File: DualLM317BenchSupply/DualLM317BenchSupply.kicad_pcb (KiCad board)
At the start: 2 copper layers, 99.1 x 150.5 mm, 40 parts, among them CON101 BARREL_JACK, CON102 BARREL_JACK, P101 CONN_1, P102 CONN_1, SW101 SPDT, SW102 SPDT, SW103 SPDT, SW201 SP6T, U101 78L05, U102 LM317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

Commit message: working on current limit switch layout
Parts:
- added D101: 1N4148, D3, F.Cu at (247.7, 257.8)
- added D102: 1N4148, D3, F.Cu at (227.3, 276.2)
- added D103: LED, LED_5MM, F.Cu at (250.2, 274.3)
- added D104: 1N4148, D3, F.Cu at (252.1, 254.6)
- added D105: 1N4148, D3, F.Cu at (250.8, 250.2)
- SW101, SW102, SW103: footprint PIN_ARRAY_3X1 -> M2012SS1W01
- moved SW101 205.2 mm to (140.3, 130.2)
- moved SW103 112.9 mm to (276.9, 186.1)
- moved SW102 104.5 mm to (257.8, 200.7)
- moved H101 50.2 mm to (139.7, 211.5)
- moved H104 50.2 mm to (232.4, 211.5)
- moved P101 50.2 mm to (195.6, 208.9)
- moved P102 50.2 mm to (176.5, 208.9)
- moved R201 50.2 mm to (143.5, 182.2)
- moved R202 50.2 mm to (148.6, 182.2)
- moved R203 50.2 mm to (146.1, 182.2)
- moved R204 50.2 mm to (170.2, 196.2)
- moved R205 50.2 mm to (170.2, 192.4)
- moved R206 50.2 mm to (170.2, 188.6)
- moved R207 50.2 mm to (170.2, 184.8)
- moved R208 50.2 mm to (152.4, 182.2)
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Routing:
- net /current_limit_r/IN: track 181.5 -> 0.00 mm
- net N-0000012: track 0.00 -> 26.5 mm
- net N-000002: track 0.00 -> 16.2 mm
- added copper zone on B.Cu, net /current_limit_r/IN
- added copper zone on B.Cu, net GND
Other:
- outline, holes or cut-outs redrawn

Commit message: working on layout
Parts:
- SW201: value SP6T -> DP6T
- moved C102 189.4 mm to (206.4, 120.0), turned to 270 degrees
- moved C103 184.1 mm to (174.6, 142.9), turned to 180 degrees
- moved U101 169.1 mm to (212.1, 120.0)
- moved R101 168.8 mm to (214.0, 126.4), turned to 180 degrees
- moved RV101 167.8 mm to (217.2, 144.8)
- moved R102 163.9 mm to (202.6, 141.6), turned to 90 degrees
- moved D102 153.7 mm to (174.0, 132.1), turned to 180 degrees
- moved D103 150.9 mm to (220.3, 126.4), turned to 180 degrees
- moved D101 147.1 mm to (166.4, 135.3), turned to 180 degrees
- moved C104 143.7 mm to (224.2, 121.3), turned to 90 degrees
- moved C105 139.3 mm to (175.3, 178.4), turned to 180 degrees
- moved C106 134.0 mm to (207.0, 137.8), turned to 90 degrees
- moved D104 129.1 mm to (200.0, 136.5), turned to 90 degrees
- moved SW102 126.3 mm to (140.3, 154.3)
- moved D105 125.6 mm to (197.5, 136.5), turned to 90 degrees
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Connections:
- net /current_limit_r/OUT renamed /current_limit_r/R_LIM-
- D101 pad 1: /current_limit_r/IN -> /current_limit_r/R_LIM+
- D102 pad 2: /current_limit_r/IN -> /current_limit_r/R_LIM+
- R204 pad 1: N-0000019 -> N-0000020
- R205 pad 1: N-0000019 -> N-0000020
- R206 pad 1: N-0000019 -> N-0000020
- R207 pad 1: N-0000019 -> N-0000020
- R209 pad 1: N-0000023 (its old number) -> N-0000019
- R210 pad 1: N-0000023 (its old number) -> N-0000019
- SW201 pad 1: /current_limit_r/IN -> /current_limit_r/R_LIM+
- SW201 pad 13: (no net) -> N-0000019
- SW201 pad 14: (no net) -> N-0000020
- SW201 pad 6: N-0000023 (its old number) -> N-0000019
- SW201 pad 7: N-0000019 -> N-0000020
- SW201 pad 8: (no net) -> /current_limit_r/R_LIM+
- U102 pad 2: /current_limit_r/IN -> /current_limit_r/R_LIM+
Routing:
- net N-000002: track 16.2 -> 139.8 mm
- net /current_limit_r/R_LIM-: track 61.8 -> 183.1 mm
- net N-000007: track 0.00 -> 86.2 mm
- net /current_limit_r/R_LIM+: track 0.00 -> 78.0 mm
- net N-0000023 (its old number): track 45.3 -> 0.00 mm
- net N-0000020: track 0.00 -> 43.3 mm
- net N-000008: track 0.00 -> 33.6 mm
- net N-000001: track 0.00 -> 24.7 mm
- net N-0000019: track 43.3 -> 18.9 mm
- net 5V: track 0.00 -> 14.2 mm
- net N-000006: track 0.00 -> 3.81 mm
- added copper zone on B.Cu, net /current_limit_r/R_LIM+
- added copper zone on B.Cu, net N-0000019
- removed copper zone on B.Cu, net /current_limit_r/IN

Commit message: pulling in diodes lib
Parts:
- P101: value CONN_1 -> Vout+
- P102: value CONN_1 -> Vout-
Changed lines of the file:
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@@
     (links 70)
     (no_connects 4)
-    (area 136.474999 114.884999 235.635001 265.480001)
+    (area 134.870999 113.280999 237.239001 265.480001)
     (thickness 1.6)
     (drawings 6)
@@
   )
   (setup
-    (last_trace_width 0.508)
+    (last_trace_width 0.254)
     (user_trace_width 0.508)
     (user_trace_width 1.016)
@@
     (pcb_text_width 0.3)
     (pcb_text_size 1.5 1.5)
-    (mod_edge_width 0.15)
+    (mod_edge_width 0.3048)
     (mod_text_size 1 1)
     (mod_text_width 0.15)
-    (pad_size 3.81 3.81)
-    (pad_drill 2.667)
+    (pad_size 2.2479 1.4986)
+    (pad_drill 0.8128)
     (pad_to_mask_clearance 0)
     (aux_axis_origin 0 0)
@@
       (layers *.Cu *.Mask F.SilkS)
       (net 4 GND)
-    )
-  )
-  (module Banana_A (layer F.Cu)
-    (at 195.58 208.915)
-    (fp_text reference P102 (at 0 6.096) (layer F.SilkS) hide
-      (effects (font (size 0.762 0.762) (thickness 0.1524)))
-    )
-    (fp_text value CONN_1 (at 0 -6.096) (layer F.SilkS)
-      (effects (font (size 0.762 0.762) (thickness 0.1524)))
-    )
-    (fp_circle (center 0 0) (end 5.334 0) (layer F.SilkS) (width 0.3048))
-    (pad 1 thru_hole circle (at 0 0) (size 9.144 9.144) (drill 6.096)
-      (layers *.Cu *.Mask F.SilkS)
-      (net 6 N-0000016)
-    )
-  )
-  (module Banana_A (layer F.Cu)
-    (at 176.53 208.915)
-    (fp_text reference P101 (at 0 6.096) (layer F.SilkS) hide
-      (effects (font (size 0.762 0.762) (thickness 0.1524)))
-    )
-    (fp_text value CONN_1 (at 0 -6.096) (layer F.SilkS)
-      (effects (font (size 0.762 0.762) (thickness 0.1524)))
-    )
-    (fp_circle (center 0 0) (end 5.334 0) (layer F.SilkS) (width 0.3048))
-    (pad 1 thru_hole circle (at 0 0) (size 9.144 9.144) (drill 6.096)
-      (layers *.Cu *.Mask F.SilkS)
-      (net 5 N-000001)
     )
   )
@@
     )
   )
+  (module Banana_A (layer F.Cu)
+    (at 176.53 208.915)
+    (fp_text reference P101 (at 0 -6) (layer F.SilkS)
+      (effects (font (size 0.762 0.762) (thickness 0.1524)))
+    )
+    (fp_text value Vout+ (at -5.715 4.445) (layer F.SilkS)
+      (effects (font (size 0.762 0.762) (thickness 0.1524)))
+    )
+    (fp_circle (center 0 0) (end 5.334 0) (layer F.SilkS) (width 0.3048))
+    (pad 1 thru_hole circle (at 0 0) (size 9.144 9.144) (drill 6.096)
+      (layers *.Cu *.Mask F.SilkS)
+      (net 5 N-000001)
+    )
+  )
+  (module Banana_A (layer F.Cu)
+    (at 195.58 208.915)
+    (fp_text reference P102 (at 0 -6) (layer F.SilkS)
+      (effects (font (size 0.762 0.762) (thickness 0.1524)))
+    )
+    (fp_text value Vout- (at 6.35 4.445) (layer F.SilkS)
+      (effects (font (size 0.762 0.762) (thickness 0.1524)))
+    )
+    (fp_circle (center 0 0) (end 5.334 0) (layer F.SilkS) (width 0.3048))
+    (pad 1 thru_hole circle (at 0 0) (size 9.144 9.144) (drill 6.096)
+      (layers *.Cu *.Mask F.SilkS)
+      (net 6 N-0000016)
+    )
+  )
   (gr_line (start 136.525 214.63) (end 235.585 214.63) (angle 90) (layer Edge.Cuts) (width 0.1))
   (gr_line (start 186.055 264.795) (end 186.055 265.43) (angle 90) (layer Edge.Cuts) (width 0.1))
@@
   (segment (start 148.59 188.16) (end 148.59 182.245) (width 1.524) (layer F.Cu) (net 14))
   (segment (start 217.805 126.365) (end 213.995 126.365) (width 0.508) (layer F.Cu) (net 15))
-  (segment (start 200.025 140.335) (end 201.295 141.605) (width 0.508) (layer F.Cu) (net 16) (status 400000))
-  (segment (start 201.295 141.605) (end 202.565 141.605) (width 0.508) (layer F.Cu) (net 16) (status 800000))
+  (segment (start 200.025 140.335) (end 201.295 141.605) (width 0.508) (layer F.Cu) (net 16))
+  (segment (start 201.295 141.605) (end 202.565 141.605) (width 0.508) (layer F.Cu) (net 16))
   (segment (start 194.31 136.525) (end 194.31 179.705) (width 3.81) (layer F.Cu) (net 16))
   (segment (start 191.135 188.595) (end 193.04 190.5) (width 3.81) (layer F.Cu) (net 16))
-  (segment (start 193.04 190.5) (end 195.58 190.5) (width 3.81) (layer F.Cu) (net 16) (status 800000))
+  (segment (start 193.04 190.5) (end 195.58 190.5) (width 3.81) (layer F.Cu) (net 16))
   (segment (start 191.135 182.88) (end 191.135 188.595) (width 3.81) (layer F.Cu) (net 16))
   (segment (start 194.31 179.705) (end 191.135 182.88) (width 3.81) (layer F.Cu) (net 16))
-  (segment (start 200.025 140.335) (end 200.025 138.43) (width 0.508) (layer F.Cu) (net 16) (status 400000))
+  (segment (start 200.025 140.335) (end 200.025 138.43) (width 0.508) (layer F.Cu) (net 16))
   (segment (start 198.12 136.525) (end 194.31 136.525) (width 0.508) (layer F.Cu) (net 16))
   (segment (start 200.025 138.43) (end 198.12 136.525) (width 0.508) (layer F.Cu) (net 16))
-  (segment (start 197.485 132.715) (end 197.485 134.62) (width 0.508) (layer F.Cu) (net 16) (status 400000))
-  (segment (start 194.31 136.525) (end 189.865 136.525) (width 2.032) (layer F.Cu) (net 16) (status 800000))
+  (segment (start 197.485 132.715) (end 197.485 134.62) (width 0.508) (layer F.Cu) (net 16))
+  (segment (start 194.31 136.525) (end 189.865 136.525) (width 2.032) (layer F.Cu) (net 16))
   (segment (start 195.58 136.525) (end 194.31 136.525) (width 0.508) (layer F.Cu) (net 16))
   (segment (start 197.485 134.62) (end 195.58 136.525) (width 0.508) (layer F.Cu) (net 16))
   (segment (start 187.96 191.77) (end 187.96 190.5) (width 1.016) (layer F.Cu) (net 16))
   (segment (start 187.96 190.5) (end 191.135 187.325) (width 1.016) (layer F.Cu) (net 16))
-  (segment (start 202.565 131.445) (end 202.565 135.89) (width 0.508) (layer F.Cu) (net 17) (status 400000))
-  (segment (start 204.47 137.795) (end 207.01 137.795) (width 0.508) (layer F.Cu) (net 17) (status 800000))
+  (segment (start 202.565 131.445) (end 202.565 135.89) (width 0.508) (layer F.Cu) (net 17))
+  (segment (start 204.47 137.795) (end 207.01 137.795) (width 0.508) (layer F.Cu) (net 17))
   (segment (start 202.565 135.89) (end 204.47 137.795) (width 0.508) (layer F.Cu) (net 17))
-  (segment (start 197.485 140.335) (end 197.485 142.24) (width 0.508) (layer F.Cu) (net 17) (status 400000))
-  (segment (start 207.01 140.335) (end 207.01 137.795) (width 0.508) (layer F.Cu) (net 17) (status 800000))
+  (segment (start 197.485 140.335) (end 197.485 142.24) (width 0.508) (layer F.Cu) (net 17))
+  (segment (start 207.01 140.335) (end 207.01 137.795) (width 0.508) (layer F.Cu) (net 17))
   (segment (start 203.835 143.51) (end 207.01 140.335) (width 0.508) (layer F.Cu) (net 17))
   (segment (start 198.755 143.51) (end 203.835 143.51) (width 0.508) (layer F.Cu) (net 17))

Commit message: updating layout
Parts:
- D101, D102, D104, D105: footprint D3 -> DIODE_3
- moved D101 3.81 mm to (170.2, 135.3)
- moved D102 3.81 mm to (177.8, 132.1)
- moved D104 3.81 mm to (200.0, 140.3)
- moved D105 3.81 mm to (197.5, 140.3)
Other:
- board size 99.1 x 150.5 mm -> 99.1 x 99.7 mm

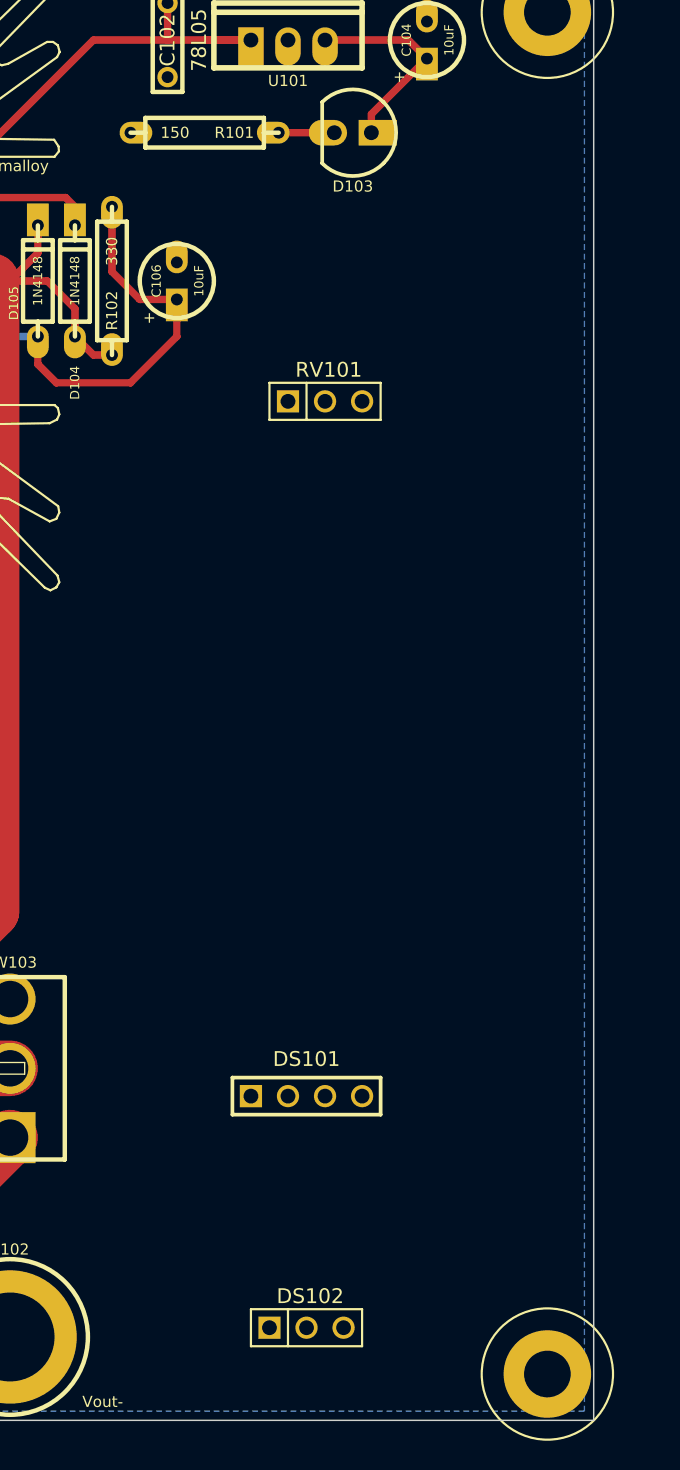
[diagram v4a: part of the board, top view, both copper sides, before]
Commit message: adding voltmeter and potentiometer to layout
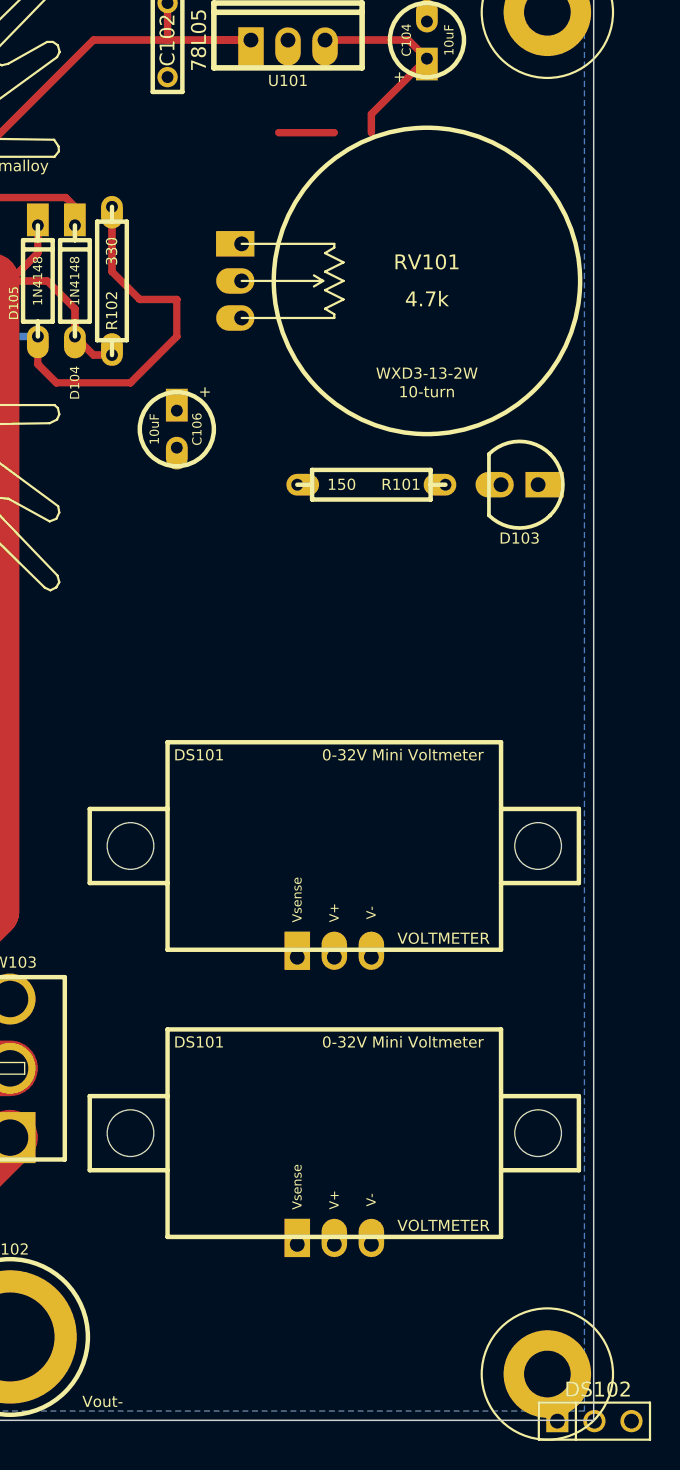
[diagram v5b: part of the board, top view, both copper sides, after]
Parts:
- removed the DS101 at (215.9, 192.4)
- added DS101: VOLTMETER, DVM036A, F.Cu at (217.8, 175.3)
- added DS101: VOLTMETER, DVM036A, F.Cu at (217.8, 194.9)
- RV101: value 4k7 -> 4.7k; footprint PIN_ARRAY_3X1 -> WXD3-13-2W_A
- moved D103 26.7 mm to (231.8, 150.5)
- moved R101 26.7 mm to (225.4, 150.5)
- moved DS102 20.7 mm to (235.6, 214.7)
- moved RV101 10.8 mm to (224.2, 136.5)
- moved C106 7.62 mm to (207.0, 145.4), turned to 270 degrees
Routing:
- net N-000006: track 3.81 -> 0.00 mm
- net (no net): track 0.00 -> 3.81 mm

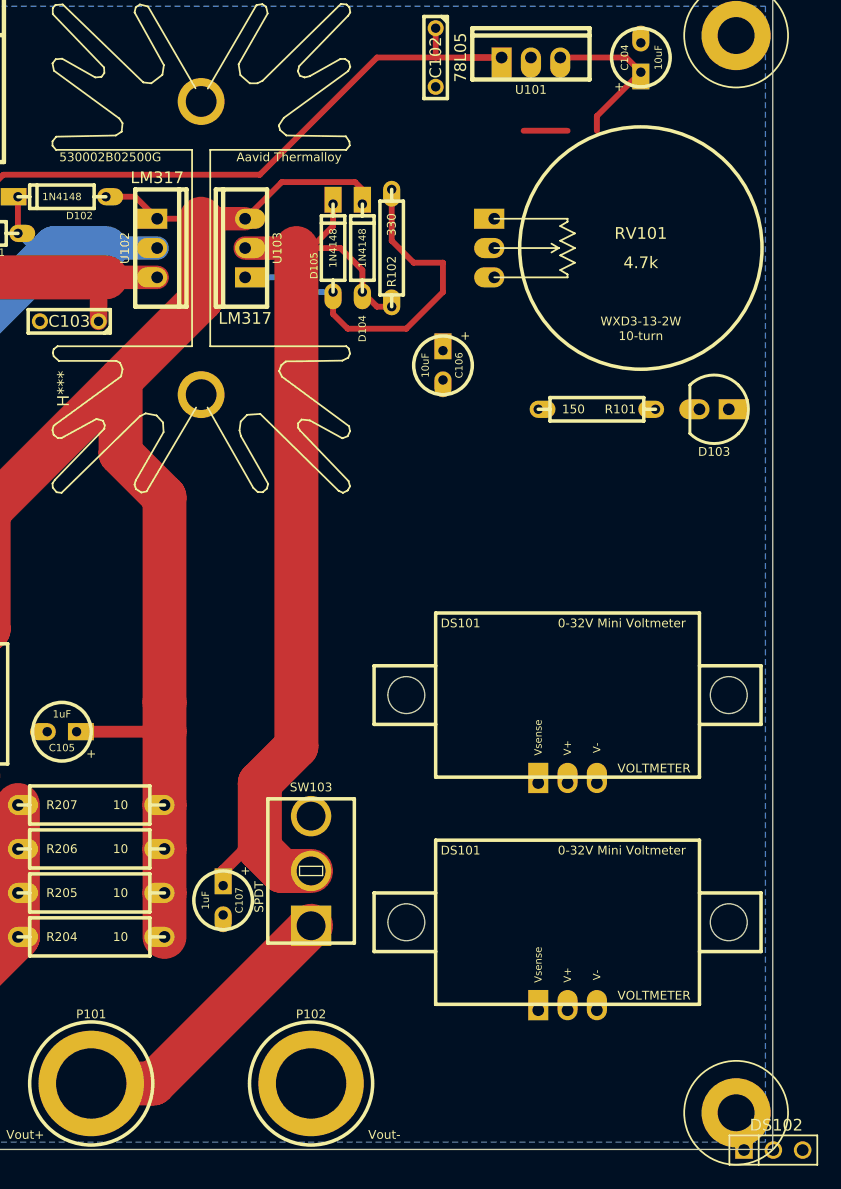
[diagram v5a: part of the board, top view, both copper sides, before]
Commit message: adding ammeter footprint
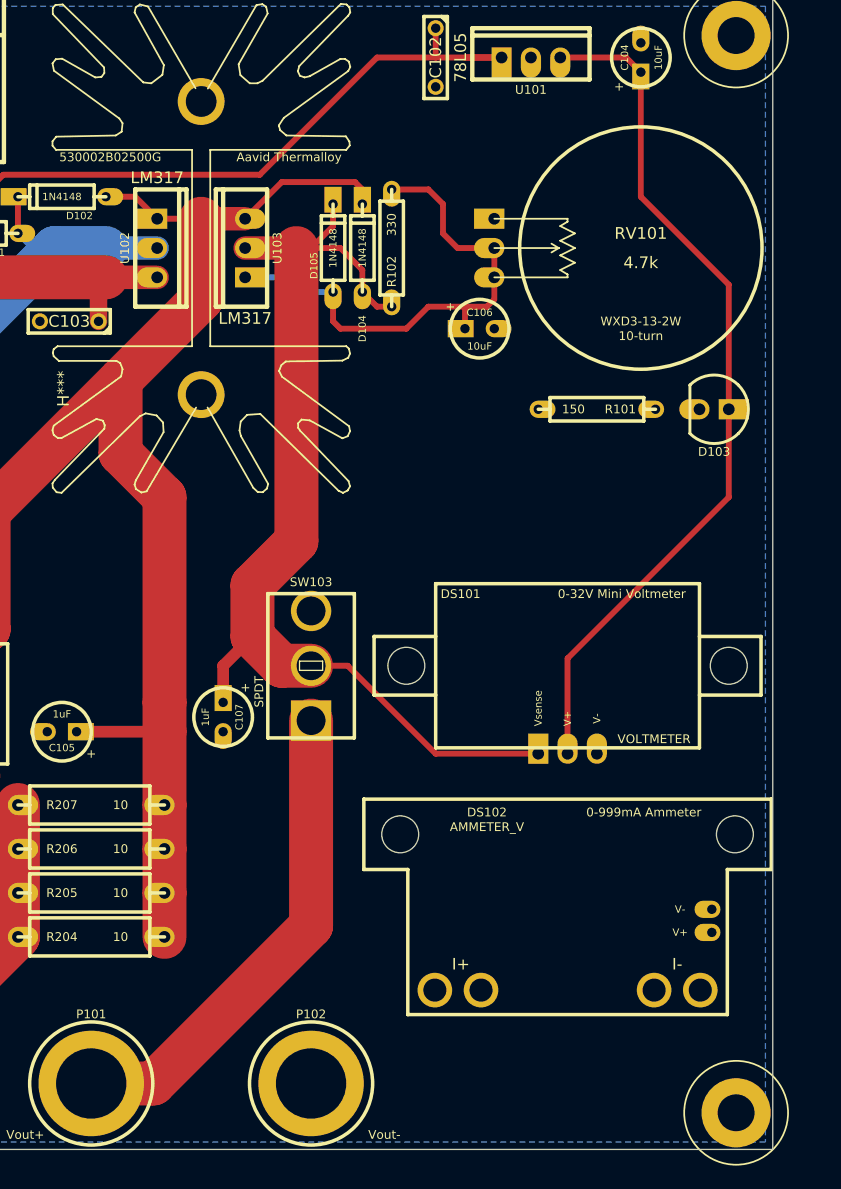
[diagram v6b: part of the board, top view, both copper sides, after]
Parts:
- removed the DS101 at (217.8, 194.9)
- DS102: footprint PIN_ARRAY_3X1 -> EBAY_AMMETER
- moved DS102 32.7 mm to (217.8, 187.3)
- moved SW103 17.8 mm to (195.6, 172.7)
- moved C107 15.9 mm to (188.0, 175.9)
- moved C106 2.69 mm to (208.9, 143.5), turned to 0 degrees
- moved DS101 2.54 mm to (217.8, 172.7)
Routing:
- net 5V: track 14.2 -> 75.5 mm
- net N-000004: track 24.7 -> 42.5 mm
- net N-000007: track 33.6 -> 44.8 mm
- net N-0000016: track 86.2 -> 92.8 mm
- net (no net): track 3.81 -> 0.00 mm
